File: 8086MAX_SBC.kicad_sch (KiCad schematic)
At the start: 17 parts, among them J1 CONN_10x2, SW1 SW_DPST_x2, U1 74HC14, U2 74HCT74, U4 74HC14, U5 74HC14

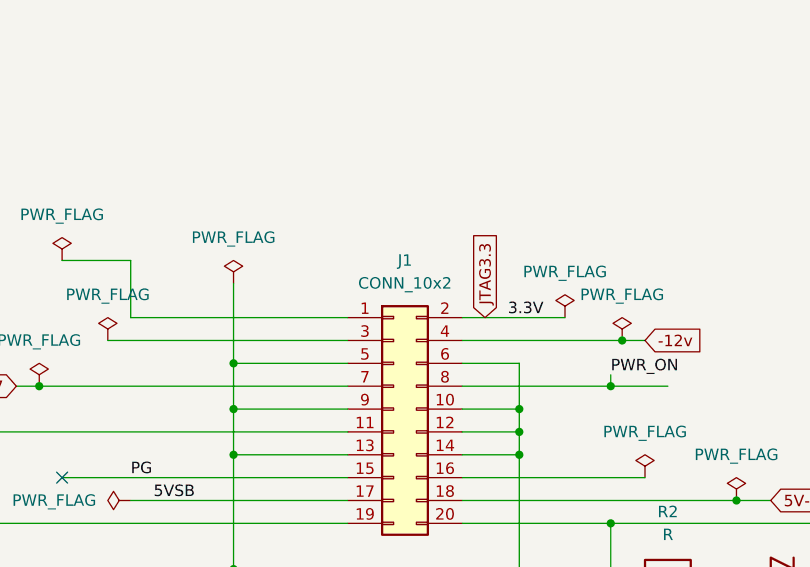
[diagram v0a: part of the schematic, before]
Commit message: Adjusted Data Bus for 80130
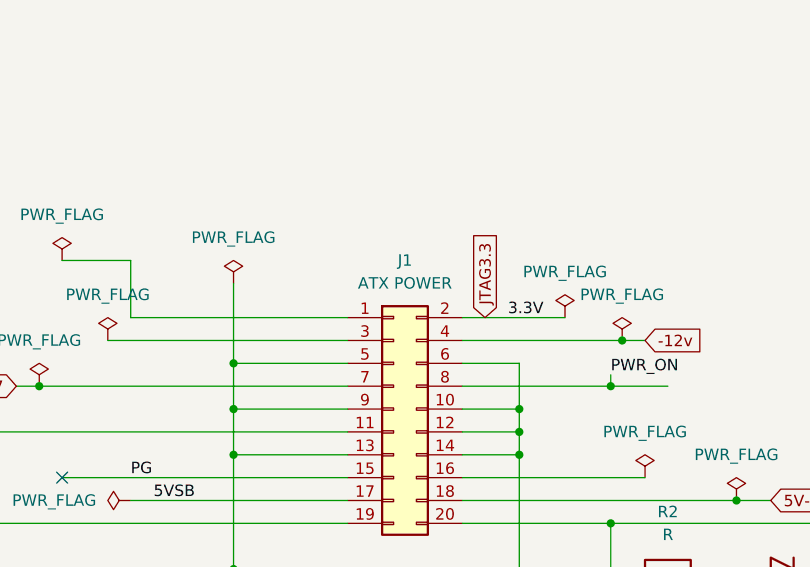
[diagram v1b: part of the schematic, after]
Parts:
- J1: value CONN_10x2 -> ATX POWER
- U1: footprint (none) -> Package_DIP:DIP-14_W7.62mm
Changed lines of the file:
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@@
 			)
 		)
-		(property "Value" "CONN_10x2"
+		(property "Value" "ATX POWER"
 			(at 186.69 113.03 0)
 			(effects
@@
 			)
 		)
-		(property "Footprint" ""
+		(property "Footprint" "Package_DIP:DIP-14_W7.62mm"
 			(at 259.08 86.36 0)
 			(effects
@@
 			)
 		)
-		(property "Footprint" ""
+		(property "Footprint" "Package_DIP:DIP-14_W7.62mm"
 			(at 118.11 55.88 0)
 			(effects
@@
 			)
 		)
-		(property "Footprint" ""
+		(property "Footprint" "Package_DIP:DIP-14_W7.62mm"
 			(at 187.96 60.96 0)
 			(effects
@@
 			)
 		)
-		(property "Footprint" ""
+		(property "Footprint" "Package_DIP:DIP-14_W7.62mm"
 			(at 212.09 60.96 0)
 			(effects
@@
 			)
 		)
-		(property "Footprint" ""
+		(property "Footprint" "Package_DIP:DIP-14_W7.62mm"
 			(at 200.66 54.61 0)
 			(effects

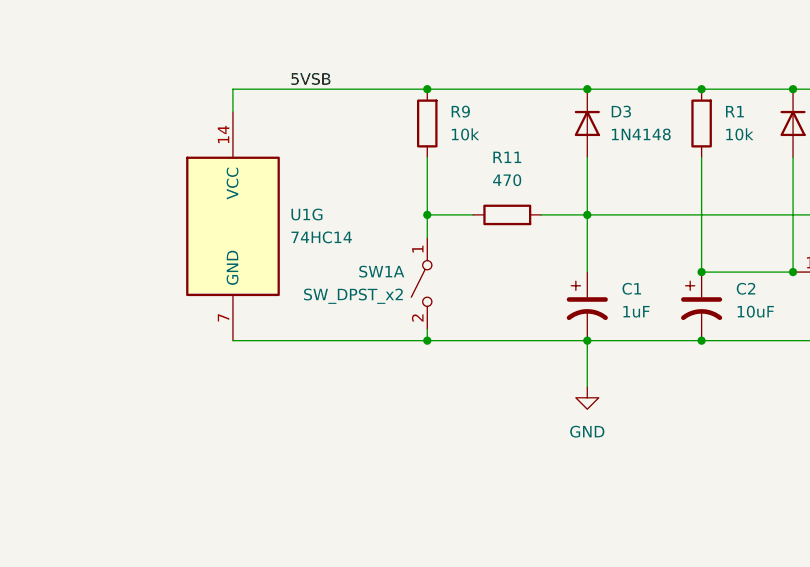
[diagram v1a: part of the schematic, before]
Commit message: assigned all footprints
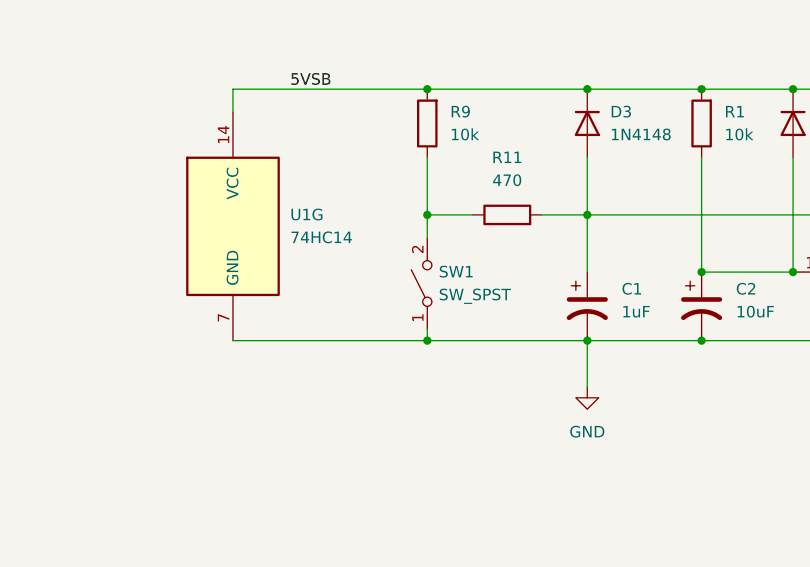
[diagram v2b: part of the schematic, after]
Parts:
- removed SW1: SW_DPST_x2, symbol Switch:SW_DPST_x2
- added SW1: SW_SPST, Button_Switch_THT:SW_Lever_1P2T_NKK_GW12LxH, symbol Switch:SW_SPST
- C1, C2: footprint (none) -> Capacitor_THT:CP_Radial_D6.3mm_P2.50mm
- C71, C72: footprint (none) -> Capacitor_THT:C_Disc_D8.0mm_W2.5mm_P5.00mm
- D2: footprint (none) -> LED_THT:LED_D5.0mm
- J1: footprint (none) -> 2-1775099-4:TE_2-1775099-4
- R1, R11, R2, R9: footprint (none) -> Resistor_THT:R_Axial_DIN0207_L6.3mm_D2.5mm_P7.62mm_Horizontal
- U2, U4, U5: footprint (none) -> Package_DIP:DIP-14_W7.62mm
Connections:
- net GND: now also SW1.1 (A)
- net at R11.1, R9.1: now also SW1.2 (B)
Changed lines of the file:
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@@
 			)
 		)
-		(property "Footprint" ""
+		(property "Footprint" "Resistor_THT:R_Axial_DIN0207_L6.3mm_D2.5mm_P7.62mm_Horizontal"
 			(at 141.478 44.45 90)
 			(effects
@@
 			)
 		)
-		(property "Footprint" ""
+		(property "Footprint" "Resistor_THT:R_Axial_DIN0207_L6.3mm_D2.5mm_P7.62mm_Horizontal"
 			(at 171.958 44.45 90)
 			(effects
@@
 			)
 		)
-		(property "Footprint" ""
+		(property "Footprint" "Capacitor_THT:C_Disc_D8.0mm_W2.5mm_P5.00mm"
 			(at 267.6652 58.42 0)
 			(effects
@@
 			)
 		)
-		(property "Footprint" ""
+		(property "Footprint" "2-1775099-4:TE_2-1775099-4"
 			(at 185.42 127 0)
 			(effects
@@
 	)
 	(symbol
-		(lib_id "Switch:SW_DPST_x2")
-		(at 139.7 62.23 90)
-		(mirror x)
-		(unit 1)
-		(exclude_from_sim no)
-		(in_bom yes)
-		(on_board yes)
-		(dnp no)
-		(property "Reference" "SW1"
-			(at 137.16 60.9599 90)
-			(effects
-				(font
-					(size 1.27 1.27)
-				)
-				(justify left)
-			)
-		)
-		(property "Value" "SW_DPST_x2"
-			(at 137.16 63.4999 90)
-			(effects
-				(font
-					(size 1.27 1.27)
-				)
-				(justify left)
-			)
-		)
-		(property "Footprint" ""
-			(at 139.7 62.23 0)
-			(effects
-				(font
-					(size 1.27 1.27)
-				)
-				(hide yes)
-			)
-		)
-		(property "Datasheet" "~"
-			(at 139.7 62.23 0)
-			(effects
-				(font
-					(size 1.27 1.27)
-				)
-				(hide yes)
-			)
-		)
-		(property "Description" "Single Pole Single Throw (SPST) switch, separate symbol"
-			(at 139.7 62.23 0)
-			(effects
-				(font
-					(size 1.27 1.27)
-				)
-				(hide yes)
-			)
-		)
-		(pin "2"
-		)
-		(pin "1"
-		)
-		(pin "4"
-		)
-		(pin "3"
-		)
-		(instances
-			(project ""
-				(path "/f3556896-fb91-4e69-9fe8-87bb2814f9d4"
-					(reference "SW1")
-					(unit 1)
-				)
-			)
-		)
-	)
-	(symbol
 		(lib_id "power:PWR_FLAG")
 		(at 213.36 134.62 0)
@@
 			)
 		)
-		(property "Footprint" ""
+		(property "Footprint" "Capacitor_THT:CP_Radial_D6.3mm_P2.50mm"
 			(at 170.18 64.77 0)
 			(effects
@@
 			)
 		)
-		(property "Footprint" ""
+		(property "Footprint" "Resistor_THT:R_Axial_DIN0207_L6.3mm_D2.5mm_P7.62mm_Horizontal"
 			(at 148.59 56.388 90)
 			(effects
@@
 			)
 		)
-		(property "Footprint" ""
+		(property "Footprint" "Resistor_THT:R_Axial_DIN0207_L6.3mm_D2.5mm_P7.62mm_Horizontal"
 			(at 215.9 146.558 90)
 			(effects
@@
 			)
 		)
-		(property "Footprint" ""
+		(property "Footprint" "LED_THT:LED_D5.0mm"
 			(at 228.6 144.78 0)
 			(effects
@@
 			)
 		)
-		(property "Footprint" ""
+		(property "Footprint" "Capacitor_THT:C_Disc_D8.0mm_W2.5mm_P5.00mm"
 			(at 256.2352 58.42 0)
 			(effects
@@
 	)
 	(symbol
+		(lib_id "Switch:SW_SPST")
+		(at 139.7 62.23 90)
+		(unit 1)
+		(exclude_from_sim no)
+		(in_bom yes)
+		(on_board yes)
+		(dnp no)
+		(fields_autoplaced yes)
+		(property "Reference" "SW1"
+			(at 140.97 60.9599 90)
+			(effects
+				(font
+					(size 1.27 1.27)
+				)
+				(justify right)
+			)
+		)
+		(property "Value" "SW_SPST"
+			(at 140.97 63.4999 90)
+			(effects
+				(font
+					(size 1.27 1.27)
+				)
+				(justify right)
+			)
+		)
+		(property "Footprint" "Button_Switch_THT:SW_Lever_1P2T_NKK_GW12LxH"
+			(at 139.7 62.23 0)
+			(effects
+				(font
+					(size 1.27 1.27)
+				)
+				(hide yes)
+			)
+		)
+		(property "Datasheet" "~"
+			(at 139.7 62.23 0)
+			(effects
+				(font
+					(size 1.27 1.27)
+				)
+				(hide yes)
+			)
+		)
+		(property "Description" "Single Pole Single Throw (SPST) switch"
+			(at 139.7 62.23 0)
+			(effects
+				(font
+					(size 1.27 1.27)
+				)
+				(hide yes)
+			)
+		)
+		(pin "2"
+		)
+		(pin "1"
+		)
+		(instances
+			(project ""
+				(path "/f3556896-fb91-4e69-9fe8-87bb2814f9d4"
+					(reference "SW1")
+					(unit 1)
+				)
+			)
+		)
+	)
+	(symbol
 		(lib_id "Device:C_Polarized_US")
 		(at 157.48 64.77 0)
@@
 			)
 		)
-		(property "Footprint" ""
+		(property "Footprint" "Capacitor_THT:CP_Radial_D6.3mm_P2.50mm"
 			(at 157.48 64.77 0)
 			(effects
@@
 			)
 		)
-		(property "Footprint" ""
+		(property "Footprint" "Package_DIP:DIP-14_W7.62mm"
 			(at 237.49 52.07 0)
 			(effects
@@
 			)
 		)
-		(property "Footprint" ""
+		(property "Footprint" "Package_DIP:DIP-14_W7.62mm"
 			(at 259.08 114.3 0)
 			(effects
@@
 			)
 		)
-		(property "Footprint" ""
+		(property "Footprint" "Package_DIP:DIP-14_W7.62mm"
 			(at 259.08 100.33 0)
 			(effects

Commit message: Updated PCB
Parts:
- removed U4, U5: 74HC14, Package_DIP:DIP-14_W7.62mm, symbol 74xx:74HC14
- added unit 3 of U2
- J1: footprint 2-1775099-4:TE_2-1775099-4 -> footprints:CONN_55660021-SD_20_MOL
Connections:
- net 5VSB: now also U2.14 (VCC)
- net GND: now also U2.7 (GND)
- no-connect marks 7 -> 3
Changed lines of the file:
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@@
 	)
 	(junction
+		(at 118.11 68.58)
+		(diameter 0)
+		(color 0 0 0 0)
+	)
+	(junction
 		(at 167.64 132.08)
 		(diameter 0)
@@
 	)
 	(junction
-		(at 209.55 124.46)
-		(diameter 0)
-		(color 0 0 0 0)
-	)
-	(junction
 		(at 135.89 139.7)
 		(diameter 0)
@@
 	)
 	(junction
+		(at 118.11 40.64)
+		(diameter 0)
+		(color 0 0 0 0)
+	)
+	(junction
 		(at 180.34 60.96)
 		(diameter 0)
@@
 	)
 	(no_connect
-		(at 251.46 114.3)
-	)
-	(no_connect
 		(at 251.46 86.36)
 	)
 	(no_connect
-		(at 266.7 100.33)
-	)
-	(no_connect
 		(at 148.59 134.62)
 	)
 	(no_connect
-		(at 266.7 114.3)
-	)
-	(no_connect
-		(at 251.46 100.33)
-	)
-	(no_connect
 		(at 266.7 86.36)
 	)
@@
 	(wire
 		(pts
-			(xy 209.55 124.46) (xy 215.9 124.46)
-		)
-		(stroke
-			(width 0)
-			(type default)
-		)
-	)
-	(wire
-		(pts
 			(xy 209.55 54.61) (xy 208.28 54.61)
 		)
@@
 	(wire
 		(pts
+			(xy 97.79 45.72) (xy 97.79 40.64)
+		)
+		(stroke
+			(width 0)
+			(type default)
+		)
+	)
+	(wire
+		(pts
 			(xy 223.52 137.16) (xy 227.33 137.16)
 		)
@@
 	(wire
 		(pts
-			(xy 193.04 124.46) (xy 209.55 124.46)
+			(xy 193.04 124.46) (xy 215.9 124.46)
 		)
 		(stroke
@@
 	(wire
 		(pts
+			(xy 97.79 68.58) (xy 118.11 68.58)
+		)
+		(stroke
+			(width 0)
+			(type default)
+		)
+	)
+	(wire
+		(pts
 			(xy 245.11 62.23) (xy 245.11 54.61)
 		)
@@
 	(wire
 		(pts
+			(xy 97.79 66.04) (xy 97.79 68.58)
+		)
+		(stroke
+			(width 0)
+			(type default)
+		)
+	)
+	(wire
+		(pts
 			(xy 157.48 40.64) (xy 170.18 40.64)
 		)
@@
 	(wire
 		(pts
-			(xy 209.55 144.78) (xy 209.55 139.7)
+			(xy 97.79 40.64) (xy 118.11 40.64)
 		)
 		(stroke
@@
 	(wire
 		(pts
-			(xy 243.84 144.78) (xy 243.84 147.32)
+			(xy 209.55 144.78) (xy 209.55 139.7)
 		)
 		(stroke
@@
 	(wire
 		(pts
-			(xy 255.27 50.8) (xy 255.27 40.64)
+			(xy 243.84 144.78) (xy 243.84 147.32)
 		)
 		(stroke
@@
 	(wire
 		(pts
-			(xy 224.79 44.45) (xy 237.49 44.45)
+			(xy 255.27 50.8) (xy 255.27 40.64)
 		)
 		(stroke
@@
 	(wire
 		(pts
-			(xy 195.58 60.96) (xy 204.47 60.96)
+			(xy 224.79 44.45) (xy 237.49 44.45)
 		)
 		(stroke
@@
 	(wire
 		(pts
-			(xy 148.59 134.62) (xy 180.34 134.62)
+			(xy 195.58 60.96) (xy 204.47 60.96)
 		)
 		(stroke
@@
 	(wire
 		(pts
-			(xy 209.55 123.19) (xy 209.55 124.46)
+			(xy 148.59 134.62) (xy 180.34 134.62)
 		)
 		(stroke
@@
 	)
 	(label "PWR_ON"
-		(at 209.55 123.19 0)
+		(at 215.9 124.46 0)
 		(effects
 			(font
@@
 	)
 	(label "PWR_ON"
-		(at 251.46 35.56 0)
+		(at 256.54 35.56 0)
 		(effects
 			(font
@@
 			)
 		)
-		(property "Footprint" "2-1775099-4:TE_2-1775099-4"
+		(property "Footprint" "footprints:CONN_55660021-SD_20_MOL"
 			(at 185.42 127 0)
 			(effects
@@
 	)
 	(symbol
+		(lib_id "74xx:74HCT74")
+		(at 97.79 55.88 0)
+		(unit 3)
+		(exclude_from_sim no)
+		(in_bom yes)
+		(on_board yes)
+		(dnp no)
+		(fields_autoplaced yes)
+		(property "Reference" "U2"
+			(at 104.14 54.6099 0)
+			(effects
+				(font
+					(size 1.27 1.27)
+				)
+				(justify left)
+			)
+		)
+		(property "Value" "74HCT74"
+			(at 104.14 57.1499 0)
+			(effects
+				(font
+					(size 1.27 1.27)
+				)
+				(justify left)
+			)
+		)
+		(property "Footprint" "Package_DIP:DIP-14_W7.62mm"
+			(at 97.79 55.88 0)
+			(effects
+				(font
+					(size 1.27 1.27)
+				)
+				(hide yes)
+			)
+		)
+		(property "Datasheet" "https://assets.nexperia.com/documents/data-sheet/74HC_HCT74.pdf"
+			(at 97.79 55.88 0)
+			(effects
+				(font
+					(size 1.27 1.27)
+				)
+				(hide yes)
+			)
+		)
+		(property "Description" "Dual D Flip-flop, Set & Reset"
+			(at 97.79 55.88 0)
+			(effects
+				(font
+					(size 1.27 1.27)
+				)
+				(hide yes)
+			)
+		)
+		(pin "3"
+		)
+		(pin "2"
+		)
+		(pin "1"
+		)
+		(pin "5"
+		)
+		(pin "12"
+		)
+		(pin "6"
+		)
+		(pin "10"
+		)
+		(pin "4"
+		)
+		(pin "13"
+		)
+		(pin "8"
+		)
+		(pin "9"
+		)
+		(pin "11"
+		)
+		(pin "14"
+		)
+		(pin "7"
+		)
+		(instances
+			(project "8086MAX_SBC"
+				(path "/f3556896-fb91-4e69-9fe8-87bb2814f9d4"
+					(reference "U2")
+					(unit 3)
+				)
+			)
+		)
+	)
+	(symbol
 		(lib_id "power:PWR_FLAG")
 		(at 204.47 116.84 0)
@@
 	(symbol
 		(lib_id "74xx:74HC14")
-		(at 259.08 114.3 0)
-		(unit 6)
-		(exclude_from_sim no)
-		(in_bom yes)
-		(on_board yes)
-		(dnp no)
-		(fields_autoplaced yes)
-		(property "Reference" "U5"
-			(at 259.08 105.41 0)
-			(effects
-				(font
-					(size 1.27 1.27)
-				)
-			)
-		)
-		(property "Value" "74HC14"
-			(at 259.08 107.95 0)
-			(effects
-				(font
-					(size 1.27 1.27)
-				)
-			)
-		)
-		(property "Footprint" "Package_DIP:DIP-14_W7.62mm"
-			(at 259.08 114.3 0)
-			(effects
-				(font
-					(size 1.27 1.27)
-				)
-				(hide yes)
-			)
-		)
-		(property "Datasheet" "http://www.ti.com/lit/gpn/sn74HC14"
-			(at 259.08 114.3 0)
-			(effects
-				(font
-					(size 1.27 1.27)
-				)
-				(hide yes)
-			)
-		)
-		(property "Description" "Hex inverter schmitt trigger"
-			(at 259.08 114.3 0)
-			(effects
-				(font
-					(size 1.27 1.27)
-				)
-				(hide yes)
-			)
-		)
-		(pin "13"
-		)
-		(pin "10"
-		)
-		(pin "8"
-		)
-		(pin "7"
-		)
-		(pin "9"
-		)
-		(pin "3"
-		)
-		(pin "1"
-		)
-		(pin "14"
-		)
-		(pin "6"
-		)
-		(pin "11"
-		)
-		(pin "4"
-		)
-		(pin "2"
-		)
-		(pin "12"
-		)
-		(pin "5"
-		)
-		(instances
-			(project "8086MAX_SBC"
-				(path "/f3556896-fb91-4e69-9fe8-87bb2814f9d4"
-					(reference "U5")
-					(unit 6)
-				)
-			)
-		)
-	)
-	(symbol
-		(lib_id "74xx:74HC14")
 		(at 200.66 54.61 0)
 		(unit 2)
@@
 				)
 			)
-		)
-	)
-	(symbol
-		(lib_id "74xx:74HC14")
-		(at 259.08 100.33 0)
-		(unit 5)
-		(exclude_from_sim no)
-		(in_bom yes)
-		(on_board yes)
-		(dnp no)
-		(fields_autoplaced yes)
-		(property "Reference" "U4"
-			(at 259.08 91.44 0)
-			(effects
-				(font
-					(size 1.27 1.27)
-				)
-			)
-		)
-		(property "Value" "74HC14"
-			(at 259.08 93.98 0)
-			(effects
-				(font
-					(size 1.27 1.27)
-				)
-			)
-		)
-		(property "Footprint" "Package_DIP:DIP-14_W7.62mm"
-			(at 259.08 100.33 0)
-			(effects
-				(font
-					(size 1.27 1.27)
-				)
-				(hide yes)
-			)
-		)
-		(property "Datasheet" "http://www.ti.com/lit/gpn/sn74HC14"
-			(at 259.08 100.33 0)
-			(effects
-				(font
-					(size 1.27 1.27)
-				)
-				(hide yes)
-			)
-		)
-		(property "Description" "Hex inverter schmitt trigger"
-			(at 259.08 100.33 0)
-			(effects
-				(font
-					(size 1.27 1.27)
-				)
-				(hide yes)
-			)
-		)
-		(pin "13"
-		)
-		(pin "10"
-		)
-		(pin "8"
-		)
-		(pin "7"
-		)
-		(pin "9"
-		)
-		(pin "3"
-		)
-		(pin "1"
-		)
-		(pin "14"
-		)
-		(pin "6"
-		)
-		(pin "11"
-		)
-		(pin "4"
-		)
-		(pin "2"
-		)
-		(pin "12"
-		)
-		(pin "5"
-		)
-		(instances
-			(project "8086MAX_SBC"
-				(path "/f3556896-fb91-4e69-9fe8-87bb2814f9d4"
-					(reference "U4")
-					(unit 5)
-				)
-			)
